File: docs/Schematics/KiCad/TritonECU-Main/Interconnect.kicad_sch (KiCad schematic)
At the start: 4 parts, among them J1 EEC-V 104

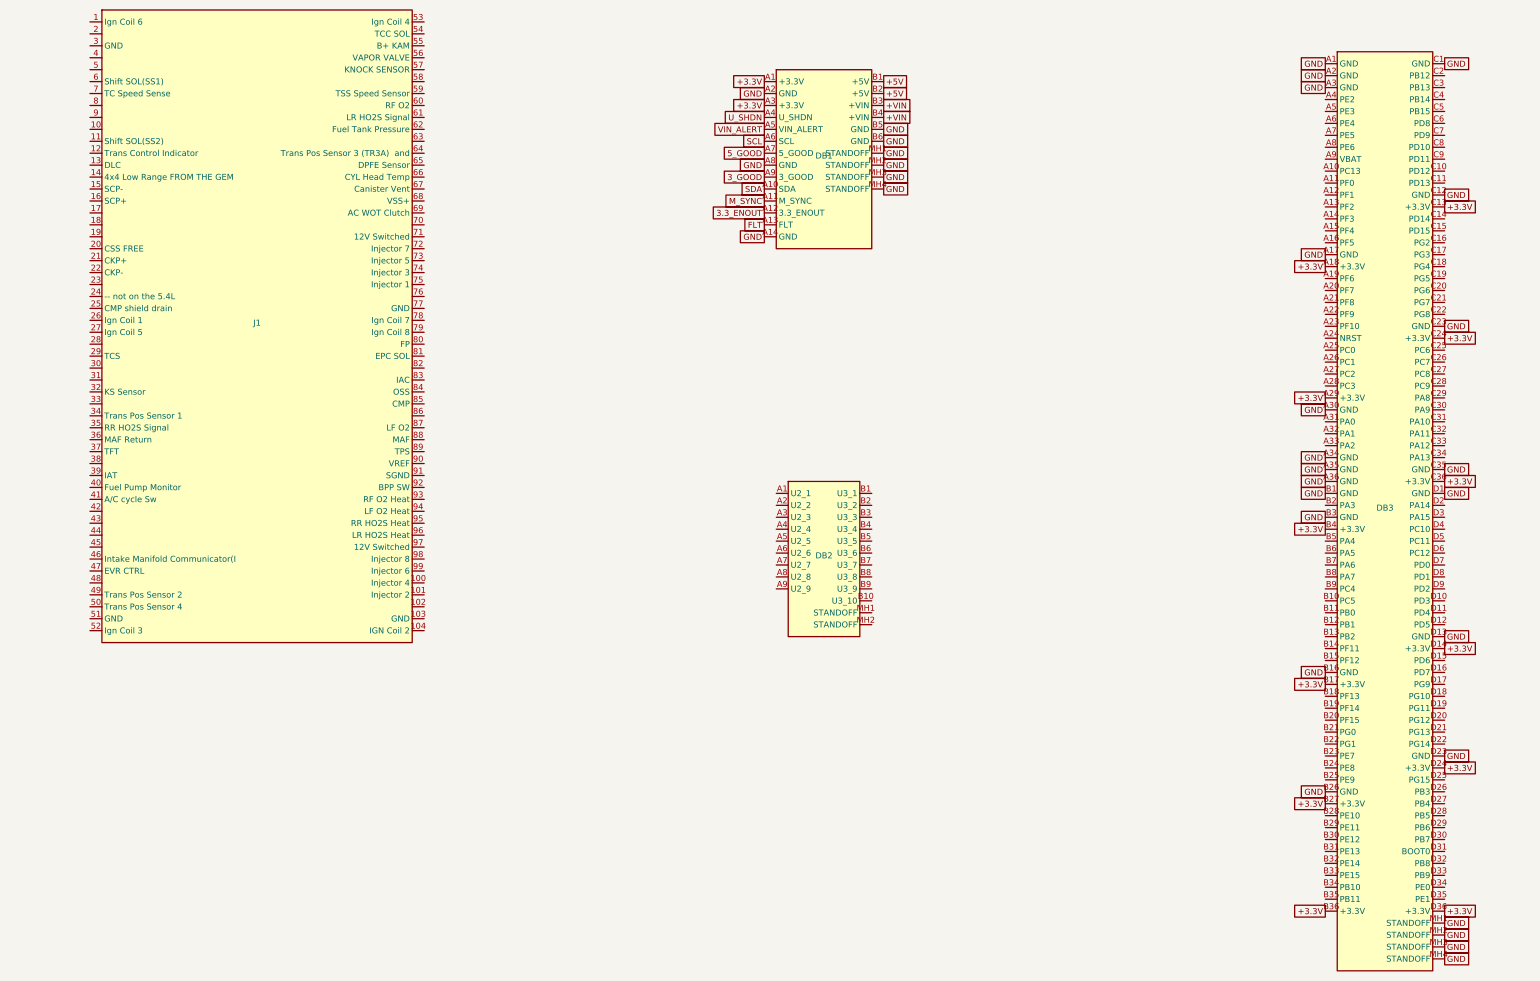
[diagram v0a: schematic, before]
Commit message: Carrier: ignition, injection and rails sheets, placed on the main board
- eecv_pins.py: the EEC-V connector map for the 5.4L, checked. Corrects SSA/SSB
  to pins 6/11: Ford's "PCM 27 (*6)" legend is * = 5.4L, and 27/1 are coils 5/6
  on this truck (schematic-ecu-v1.txt and measurements-wanted.md fixed).
- carrier_pinmap.py: adds TCS (O/D cancel, pin 29) on PE1, polled; 4x4-low has
  no PCM pin in either source, marked [CONFIRM]. 100 signals, 5 spare.
- Interconnect sheet rebuilt every run with every connector and module pin
  labelled from the two maps (symbol UUIDs kept); deliberate no-connects flagged.
- gen_carrier.py: Rails, Ignition (74HCT541, 8x ISL9V3040, TPS3823A-33 watchdog
  on NRST and OE2 via BSS138, JP101 v1 strap) and Injection (8x ZXMS6005DGQ,
  10k input pulldowns). Deterministic symbol UUIDs keep the PCB linked. Own
  symbols for the IntelliFET (the Samacsys import is broken) and NCV8772.
- gen_carrier_pcb.py: adds missing parts to the board linked to their symbols,
  sets every pad net from the netlist, places a first-draft floor plan by
  connector position. DRC: no courtyard overlaps, schematic parity clean.
- ADC goes back on the carrier: adc-daughterboard.md superseded.

Co-Authored-By: Claude Opus 5.5 <noreply@anthropic.com>
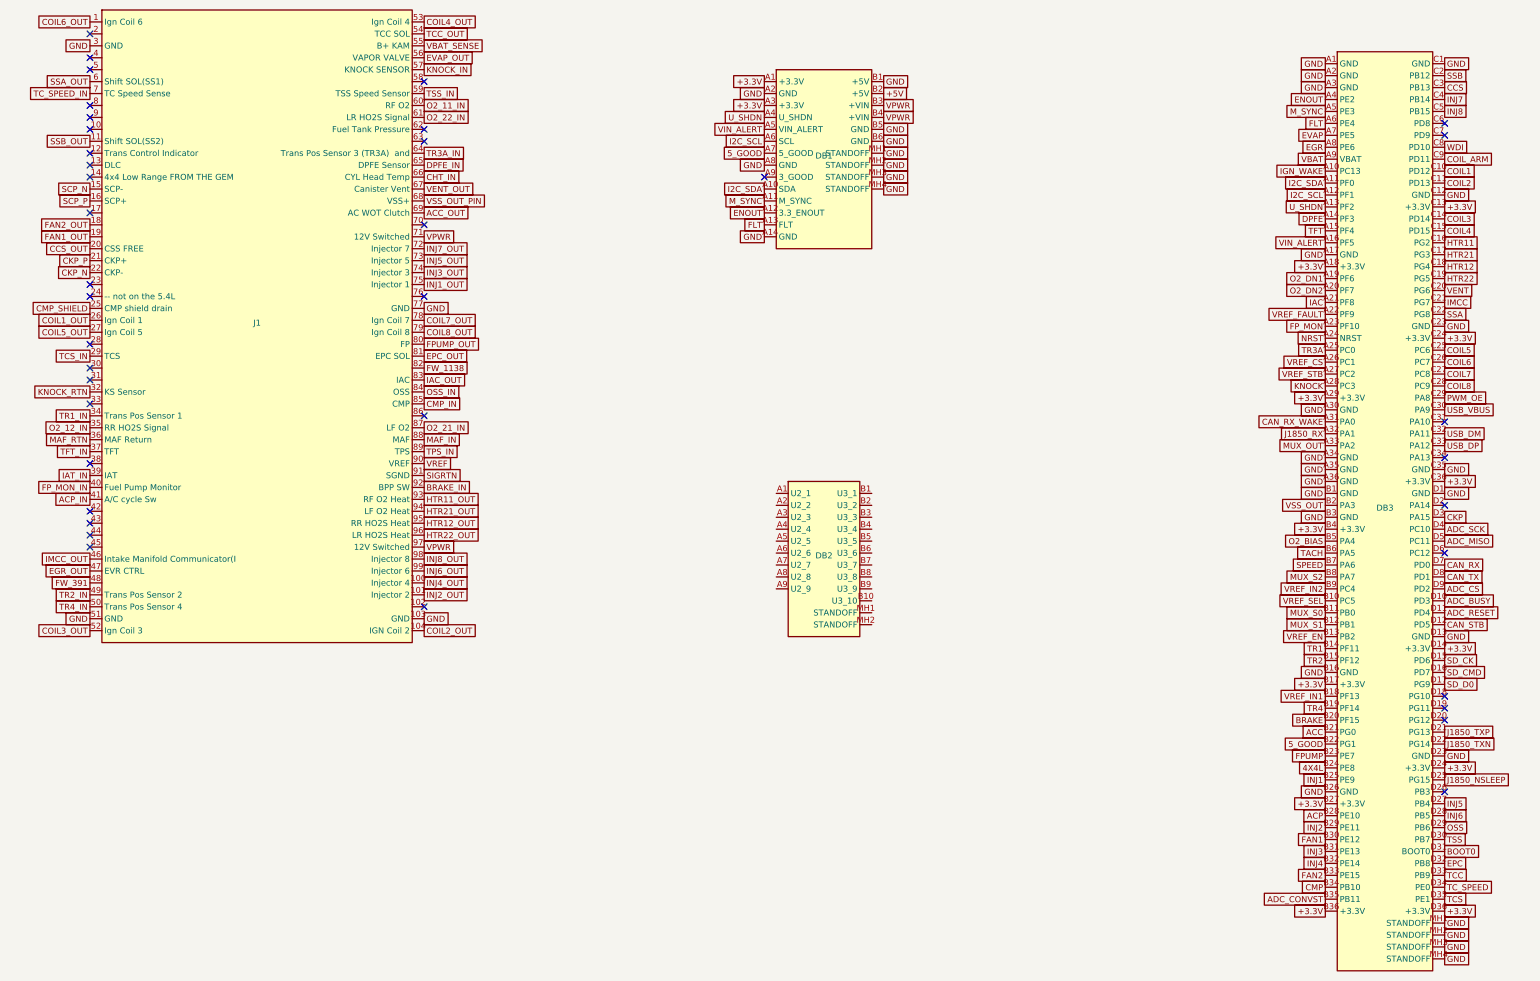
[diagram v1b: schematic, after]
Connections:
- net +VIN is gone; now on net VPWR: DB1.B3 (+VIN), DB1.B4 (+VIN)
- net 3.3_ENOUT is gone; now on net ENOUT: DB1.A12 (3.3_ENOUT)
- net SCL is gone; now on net I2C_SCL: DB1.A6 (SCL)
- net SDA is gone; now on net I2C_SDA: DB1.A10 (SDA)
- net +5V: no longer DB1.B1 (+5V)
- net 5_GOOD: now also DB3.B22 (PG1)
- net FLT: now also DB3.A6 (PE4)
- net GND: now also DB1.B1 (+5V), J1.103 (GND), J1.3 (GND), J1.51 (GND), J1.77 (GND)
- net M_SYNC: now also DB3.A5 (PE3)
- net U_SHDN: now also DB3.A13 (PF2)
- net VIN_ALERT: now also DB3.A16 (PF5)
- net COIL6_OUT: now reaches J1.1 (Ign Coil 6)
- net INJ4_OUT: now reaches J1.100 (Injector 4)
- net INJ2_OUT: now reaches J1.101 (Injector 2)
- net COIL2_OUT: now reaches J1.104 (IGN Coil 2)
- net SSB_OUT: now reaches J1.11 (Shift SOL(SS2))
- net SCP_N: now reaches J1.15 (SCP-)
- net SCP_P: now reaches J1.16 (SCP+)
- net FAN2_OUT: now reaches J1.18
- net FAN1_OUT: now reaches J1.19
- net CCS_OUT: now reaches J1.20 (CSS FREE)
- net CKP_P: now reaches J1.21 (CKP+)
- net CKP_N: now reaches J1.22 (CKP-)
- net CMP_SHIELD: now reaches J1.25 (CMP shield drain)
- net COIL1_OUT: now reaches J1.26 (Ign Coil 1)
- net COIL5_OUT: now reaches J1.27 (Ign Coil 5)
- net TCS_IN: now reaches J1.29 (TCS)
- net KNOCK_RTN: now reaches J1.32 (KS Sensor)
- net TR1_IN: now reaches J1.34 (Trans Pos Sensor 1)
- net O2_12_IN: now reaches J1.35 (RR HO2S Signal)
- net MAF_RTN: now reaches J1.36 (MAF Return)
- net TFT_IN: now reaches J1.37 (TFT)
- net IAT_IN: now reaches J1.39 (IAT)
- net FP_MON_IN: now reaches J1.40 (Fuel Pump Monitor)
- net ACP_IN: now reaches J1.41 (A/C cycle Sw)
- net IMCC_OUT: now reaches J1.46 (Intake Manifold Communicator(I)
- net EGR_OUT: now reaches J1.47 (EVR CTRL)
- net FW_391: now reaches J1.48
- net TR2_IN: now reaches J1.49 (Trans Pos Sensor 2)
- net TR4_IN: now reaches J1.50 (Trans Pos Sensor 4)
- net COIL3_OUT: now reaches J1.52 (Ign Coil 3)
- net COIL4_OUT: now reaches J1.53 (Ign Coil 4)
- net TCC_OUT: now reaches J1.54 (TCC SOL)
- net VBAT_SENSE: now reaches J1.55 (B+ KAM)
- net EVAP_OUT: now reaches J1.56 (VAPOR VALVE)
- net KNOCK_IN: now reaches J1.57 (KNOCK SENSOR)
- net TSS_IN: now reaches J1.59 (TSS Speed Sensor)
- net SSA_OUT: now reaches J1.6 (Shift SOL(SS1))
- net O2_11_IN: now reaches J1.60 (RF O2)
- net O2_22_IN: now reaches J1.61 (LR HO2S Signal)
- net TR3A_IN: now reaches J1.64 (Trans Pos Sensor 3 (TR3A)  and)
- net DPFE_IN: now reaches J1.65 (DPFE Sensor)
- net CHT_IN: now reaches J1.66 (CYL Head Temp)
- net VENT_OUT: now reaches J1.67 (Canister Vent)
- net VSS_OUT_PIN: now reaches J1.68 (VSS+)
- net ACC_OUT: now reaches J1.69 (AC WOT Clutch)
- net TC_SPEED_IN: now reaches J1.7 (TC Speed Sense)
- net VPWR: now reaches J1.71 (12V Switched)
- net VPWR: now also J1.97 (12V Switched)
- net INJ7_OUT: now reaches J1.72 (Injector 7)
- net INJ5_OUT: now reaches J1.73 (Injector 5)
- net INJ3_OUT: now reaches J1.74 (Injector 3)
- net INJ1_OUT: now reaches J1.75 (Injector 1)
- net COIL7_OUT: now reaches J1.78 (Ign Coil 7)
- net COIL8_OUT: now reaches J1.79 (Ign Coil 8)
- net FPUMP_OUT: now reaches J1.80 (FP)
- net EPC_OUT: now reaches J1.81 (EPC SOL)
- net FW_1138: now reaches J1.82
- net IAC_OUT: now reaches J1.83 (IAC)
- net OSS_IN: now reaches J1.84 (OSS)
- net CMP_IN: now reaches J1.85 (CMP)
- net O2_21_IN: now reaches J1.87 (LF O2)
- net MAF_IN: now reaches J1.88 (MAF)
- net TPS_IN: now reaches J1.89 (TPS)
- net VREF: now reaches J1.90 (VREF)
- net SIGRTN: now reaches J1.91 (SGND)
- net BRAKE_IN: now reaches J1.92 (BPP SW)
- net HTR11_OUT: now reaches J1.93 (RF O2 Heat)
- net HTR21_OUT: now reaches J1.94 (LF O2 Heat)
- net HTR12_OUT: now reaches J1.95 (RR HO2S Heat)
- net HTR22_OUT: now reaches J1.96 (LR HO2S Heat)
- net INJ8_OUT: now reaches J1.98 (Injector 8)
- net INJ6_OUT: now reaches J1.99 (Injector 6)
- net IGN_WAKE: now reaches DB3.A10 (PC13)
- net I2C_SDA: now reaches DB3.A11 (PF0)
- net I2C_SCL: now reaches DB3.A12 (PF1)
- net DPFE: now reaches DB3.A14 (PF3)
- net TFT: now reaches DB3.A15 (PF4)
- net O2_DN1: now reaches DB3.A19 (PF6)
- net O2_DN2: now reaches DB3.A20 (PF7)
- net IAC: now reaches DB3.A21 (PF8)
- net VREF_FAULT: now reaches DB3.A22 (PF9)
- net FP_MON: now reaches DB3.A23 (PF10)
- net NRST: now reaches DB3.A24 (NRST)
- net TR3A: now reaches DB3.A25 (PC0)
- net VREF_CS: now reaches DB3.A26 (PC1)
- net VREF_STB: now reaches DB3.A27 (PC2)
- net KNOCK: now reaches DB3.A28 (PC3)
- net CAN_RX_WAKE: now reaches DB3.A31 (PA0)
- net J1850_RX: now reaches DB3.A32 (PA1)
- net MUX_OUT: now reaches DB3.A33 (PA2)
- net ENOUT: now reaches DB3.A4 (PE2)
- net EVAP: now reaches DB3.A7 (PE5)
- net EGR: now reaches DB3.A8 (PE6)
- net VBAT: now reaches DB3.A9 (VBAT)
- net VREF_SEL: now reaches DB3.B10 (PC5)
- net MUX_S0: now reaches DB3.B11 (PB0)
- net MUX_S1: now reaches DB3.B12 (PB1)
- net VREF_EN: now reaches DB3.B13 (PB2)
- net TR1: now reaches DB3.B14 (PF11)
- net TR2: now reaches DB3.B15 (PF12)
- net VREF_IN1: now reaches DB3.B18 (PF13)
- net TR4: now reaches DB3.B19 (PF14)
- net VSS_OUT: now reaches DB3.B2 (PA3)
- net BRAKE: now reaches DB3.B20 (PF15)
- net ACC: now reaches DB3.B21 (PG0)
- net FPUMP: now reaches DB3.B23 (PE7)
- net 4X4L: now reaches DB3.B24 (PE8)
- net INJ1: now reaches DB3.B25 (PE9)
- net ACP: now reaches DB3.B28 (PE10)
- net INJ2: now reaches DB3.B29 (PE11)
- net FAN1: now reaches DB3.B30 (PE12)
- net INJ3: now reaches DB3.B31 (PE13)
- net INJ4: now reaches DB3.B32 (PE14)
- net FAN2: now reaches DB3.B33 (PE15)
- net CMP: now reaches DB3.B34 (PB10)
- net ADC_CONVST: now reaches DB3.B35 (PB11)
- net O2_BIAS: now reaches DB3.B5 (PA4)
- net TACH: now reaches DB3.B6 (PA5)
- net SPEED: now reaches DB3.B7 (PA6)
- net MUX_S2: now reaches DB3.B8 (PA7)
- net VREF_IN2: now reaches DB3.B9 (PC4)
- net COIL1: now reaches DB3.C10 (PD12)
- net COIL2: now reaches DB3.C11 (PD13)
- net COIL3: now reaches DB3.C14 (PD14)
- net COIL4: now reaches DB3.C15 (PD15)
- net HTR11: now reaches DB3.C16 (PG2)
- net HTR21: now reaches DB3.C17 (PG3)
- net HTR12: now reaches DB3.C18 (PG4)
- net HTR22: now reaches DB3.C19 (PG5)
- net SSB: now reaches DB3.C2 (PB12)
- net VENT: now reaches DB3.C20 (PG6)
- net IMCC: now reaches DB3.C21 (PG7)
- net SSA: now reaches DB3.C22 (PG8)
- net COIL5: now reaches DB3.C25 (PC6)
- net COIL6: now reaches DB3.C26 (PC7)
- net COIL7: now reaches DB3.C27 (PC8)
- net COIL8: now reaches DB3.C28 (PC9)
- net PWM_OE: now reaches DB3.C29 (PA8)
- net CCS: now reaches DB3.C3 (PB13)
- net USB_VBUS: now reaches DB3.C30 (PA9)
- net USB_DM: now reaches DB3.C32 (PA11)
- net USB_DP: now reaches DB3.C33 (PA12)
- net INJ7: now reaches DB3.C4 (PB14)
- net INJ8: now reaches DB3.C5 (PB15)
- net WDI: now reaches DB3.C8 (PD10)
- net COIL_ARM: now reaches DB3.C9 (PD11)
- net ADC_BUSY: now reaches DB3.D10 (PD3)
- net ADC_RESET: now reaches DB3.D11 (PD4)
- net CAN_STB: now reaches DB3.D12 (PD5)
- net SD_CK: now reaches DB3.D15 (PD6)
- net SD_CMD: now reaches DB3.D16 (PD7)
- net SD_D0: now reaches DB3.D17 (PG9)
- net J1850_TXP: now reaches DB3.D21 (PG13)
- net J1850_TXN: now reaches DB3.D22 (PG14)
- net J1850_NSLEEP: now reaches DB3.D25 (PG15)
- net INJ5: now reaches DB3.D27 (PB4)
- net INJ6: now reaches DB3.D28 (PB5)
- net OSS: now reaches DB3.D29 (PB6)
- net CKP: now reaches DB3.D3 (PA15)
- net TSS: now reaches DB3.D30 (PB7)
- net BOOT0: now reaches DB3.D31 (BOOT0)
- net EPC: now reaches DB3.D32 (PB8)
- net TCC: now reaches DB3.D33 (PB9)
- net TC_SPEED: now reaches DB3.D34 (PE0)
- net TCS: now reaches DB3.D35 (PE1)
- net ADC_SCK: now reaches DB3.D4 (PC10)
- net ADC_MISO: now reaches DB3.D5 (PC11)
- net CAN_RX: now reaches DB3.D7 (PD0)
- net CAN_TX: now reaches DB3.D8 (PD1)
- net ADC_CS: now reaches DB3.D9 (PD2)
- net 3_GOOD: no longer names the net of DB1.A9 (3_GOOD)
- no-connect marks 0 -> 39

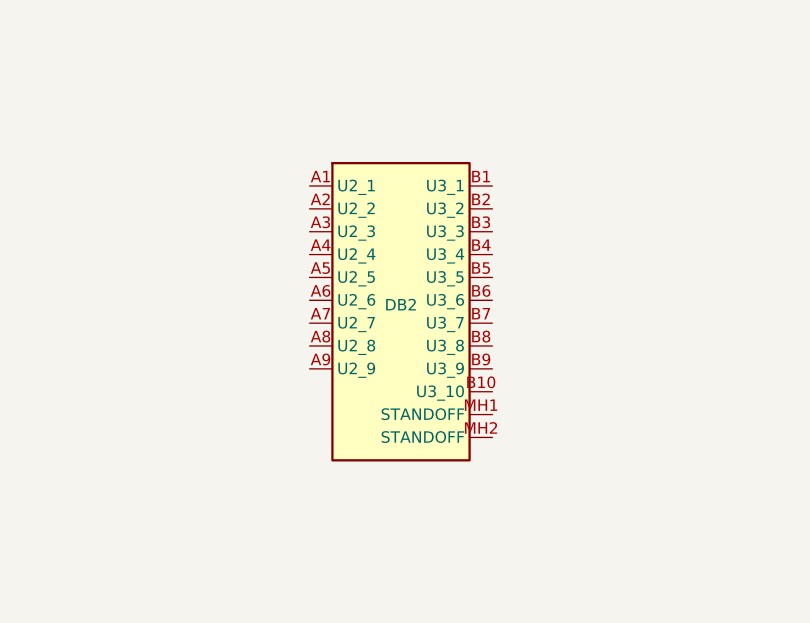
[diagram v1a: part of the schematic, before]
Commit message: Carrier: VR front end on the main board, 3 x MAX9926
The VR daughterboard (DB2) is removed; the conditioning moves onto the carrier
as Vr.kicad_sch, U301-U303: CKP + spare, CMP + OSS, TSS + transfer case. All
V1 review fixes applied: 2 x 5k 0805 per input leg (300 V), 470 pF C0G 200 V
across the inputs, 100 nF on BIAS, 10n + 100n + 1u per VCC. Single-ended
sensors return on SIGRTN; the CMP shield goes single-point to the star through
R399; the spare channel is on header J301. VR board V1 stays the bench board.

Placed where DB2 was, under the CMP/OSS/TSS/TC pins. ERC 0 errors, PCB
schematic parity clean, no courtyard overlaps.

Generators: lock check ignores the project window alone; stale footprints are
removed after the new ones load (a Remove first broke the footprint loader).

Co-Authored-By: Claude Opus 5.5 <noreply@anthropic.com>
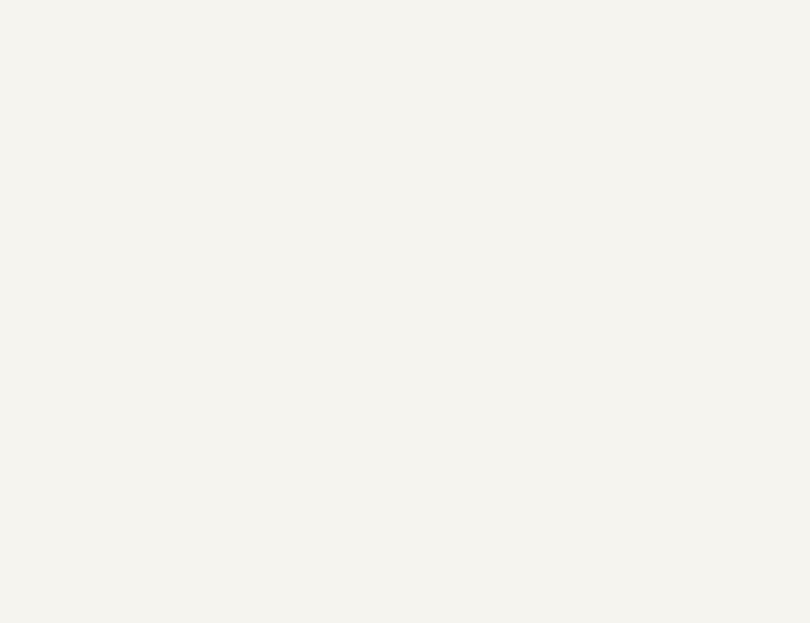
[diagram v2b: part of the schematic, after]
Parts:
- removed DB2: VR board V1, TritonECU-Main:VRBoard_V1_Mate, symbol TritonECU-Main:VRBoard_V1_Mate

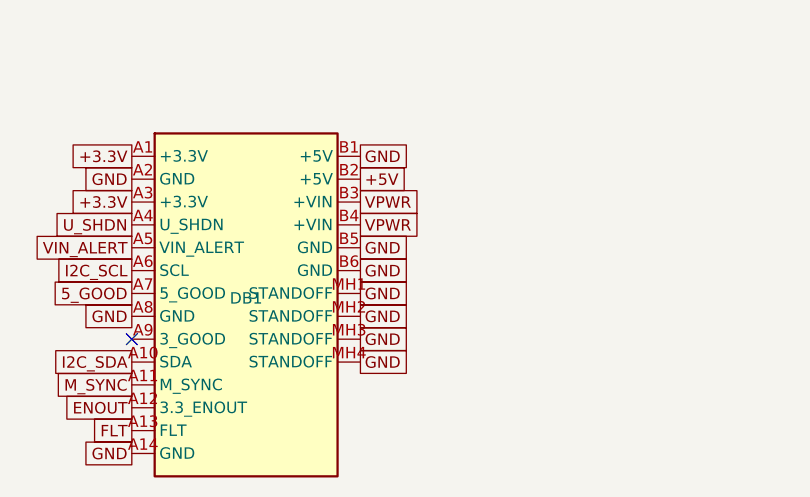
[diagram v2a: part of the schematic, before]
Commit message: Carrier: VREF sheet, and the power board's +VIN is VPROT, not VPWR
VREF: NCV8772C 5.00 V on the protected rail, EN from the MCU; TPS2H160B-Q1
at 248 mA per feed, latch mode; LM74700-Q1 + DMN6040 ideal diode and
SMAJ24CA per feed; 100k/12.4k short-to-battery sense. Channel 2 drawn,
not fitted (one VREF pin, 90).

Fix: power board J3 +VIN is the LTC4364 OUTPUT (IC1 pin 1, after R2).
The carrier had it on VPWR, joining the surge stopper's output to its
raw input. It is now its own net, VPROT, which also feeds VREF.

gen_carrier_pcb.py: no-connect pins get their unconnected net (parity),
and --replace-sheet NAME re-places one sheet's parts.

Co-Authored-By: Claude Opus 5.5 <noreply@anthropic.com>
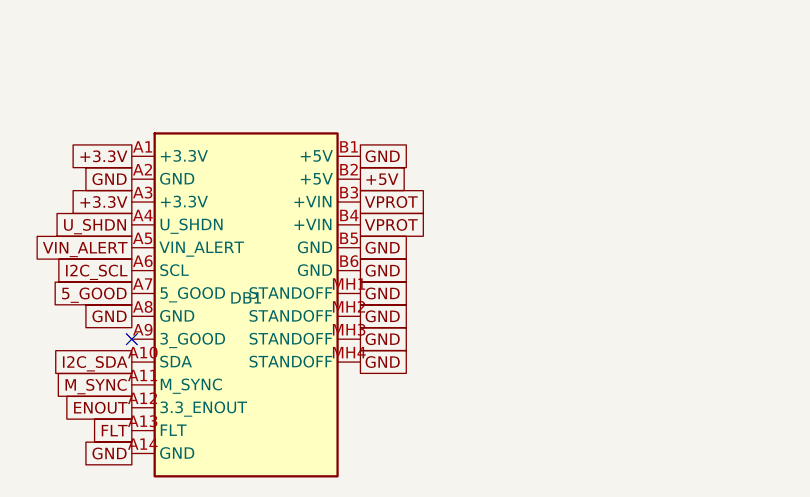
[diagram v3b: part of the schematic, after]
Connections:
- net VPWR: no longer DB1.B3 (+VIN), DB1.B4 (+VIN)
- new net VPROT: DB1.B3 (+VIN), DB1.B4 (+VIN)

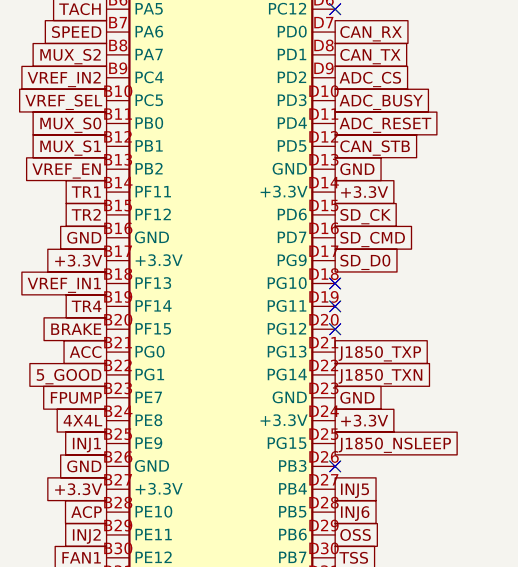
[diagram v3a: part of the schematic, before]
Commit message: Carrier: ADC sheet (ADS8588H, reference, HO2S buffers, knock, slow channels)
ADS8588H serial on DOUTA, +-10 V, external MAX6070AAUT25 gated by the new
ADC_REF_EN (PG10). MAF differential on ch 1, battery 180k/30k on pin 55,
VREF_5V on ch 8. HO2S x4 per o2-input-stage.md on OPA2376. Knock charge
amp on TLV9064, moved to +3.3 V with a 1.8 V VMID because it lands on a
3.3 V MCU ADC pin. DPFE, TFT, FP monitor conditioned for the MCU ADC.
Series R on the unbuffered channels fitted 0R pending [DECIDE].

gen_carrier_pcb.py: PACK groups placed by courtyard shelf packing.
gen_carrier.py: own dual/quad op-amp symbols, fills an empty placeholder
sheet and keeps its block uuid.

Co-Authored-By: Claude Opus 5.5 <noreply@anthropic.com>
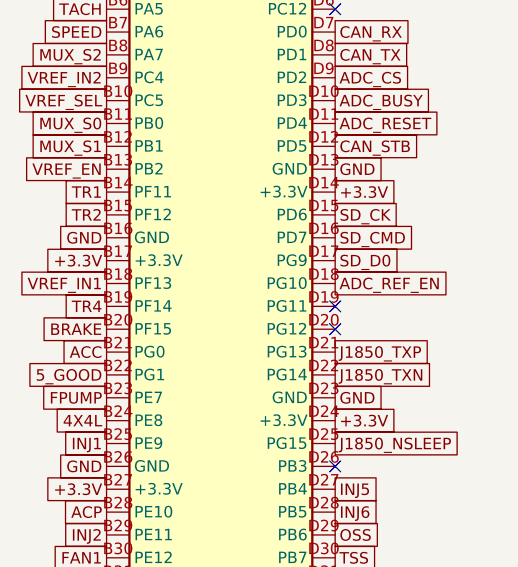
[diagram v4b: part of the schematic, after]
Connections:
- net ADC_REF_EN: now reaches DB3.D18 (PG10)
- no-connect marks 39 -> 38
